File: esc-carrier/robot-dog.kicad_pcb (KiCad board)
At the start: 2 copper layers, 35 parts, among them J1 Conn_01x02, J10 Conn_01x02, J11 Conn_01x04, J12 Conn_01x04, J13 Conn_01x04, J2 Conn_01x04, J3 Conn_01x04, J4 Conn_01x03, J5 Conn_01x05, J6 Conn_01x05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

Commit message: start trace routing
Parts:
- moved R4 43.6 mm to (155.2, 58.4)
- moved R5 43.6 mm to (155.2, 99.1)
- moved R6 43.6 mm to (155.2, 139.7)
- moved SW1 17.2 mm to (195.9, 43.3)
- moved D1 8.64 mm to (213.4, 54.1)
- moved R1 8.64 mm to (213.4, 51.7)
- moved J3 8.62 mm to (185.5, 115.8)
- moved J2 8.62 mm to (185.5, 75.2)
- moved J9 7.95 mm to (183.1, 93.9)
- moved J13 7.88 mm to (192.2, 140.6)
- moved R11 7.88 mm to (209.2, 140.6)
- moved J11 7.88 mm to (192.2, 59.3)
- moved J12 7.88 mm to (192.2, 99.9)
- moved J10 7.88 mm to (183.1, 134.5)
- moved J7 7.88 mm to (181.5, 140.6)
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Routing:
- net +12V: track 0.00 -> 256.4 mm, vias 0 -> 3
- net +5V: track 0.00 -> 251.6 mm, vias 0 -> 5
- net VCC: track 0.00 -> 241.6 mm, vias 0 -> 1
- net SDA: track 0.00 -> 205.1 mm, vias 0 -> 3
- net SCL: track 0.00 -> 196.6 mm, vias 0 -> 3
- net Net-(J11-Pad1): track 0.00 -> 196.4 mm, vias 0 -> 3
- net Net-(J11-Pad2): track 0.00 -> 185.1 mm, vias 0 -> 3
- net Net-(J7-Pad1): track 0.00 -> 27.3 mm
- net Net-(J6-Pad1): track 0.00 -> 26.3 mm
- net Net-(J5-Pad1): track 0.00 -> 26.3 mm
- net Net-(J13-Pad3): track 0.00 -> 18.9 mm
- net Net-(J12-Pad3): track 0.00 -> 18.3 mm
- net Net-(J11-Pad3): track 0.00 -> 18.3 mm
- net Net-(J12-Pad4): track 0.00 -> 14.0 mm
- net Net-(J11-Pad4): track 0.00 -> 14.0 mm
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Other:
- board outline added: 87.6 x 110.5 mm
- board text added: "12V"
- board text added: "5V"
- board text added: "VCC"

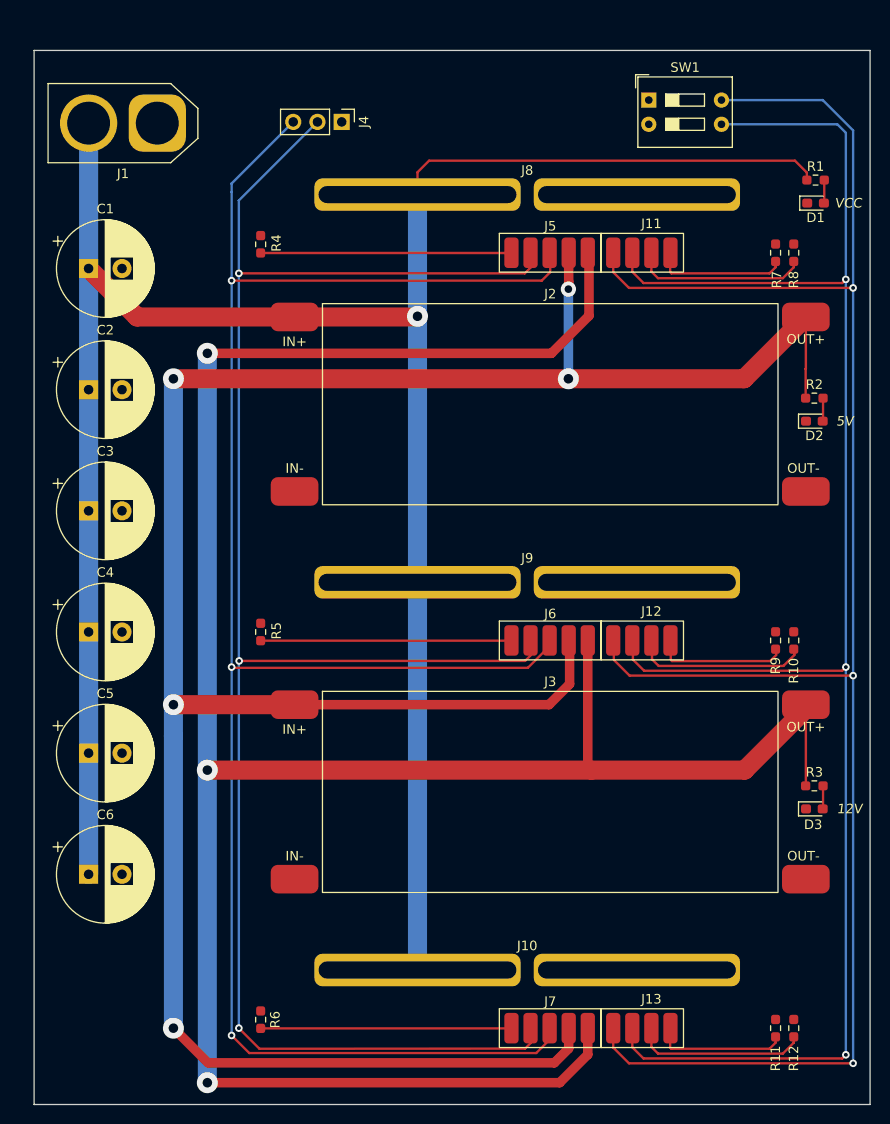
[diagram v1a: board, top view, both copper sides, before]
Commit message: fix intersecting courtyard
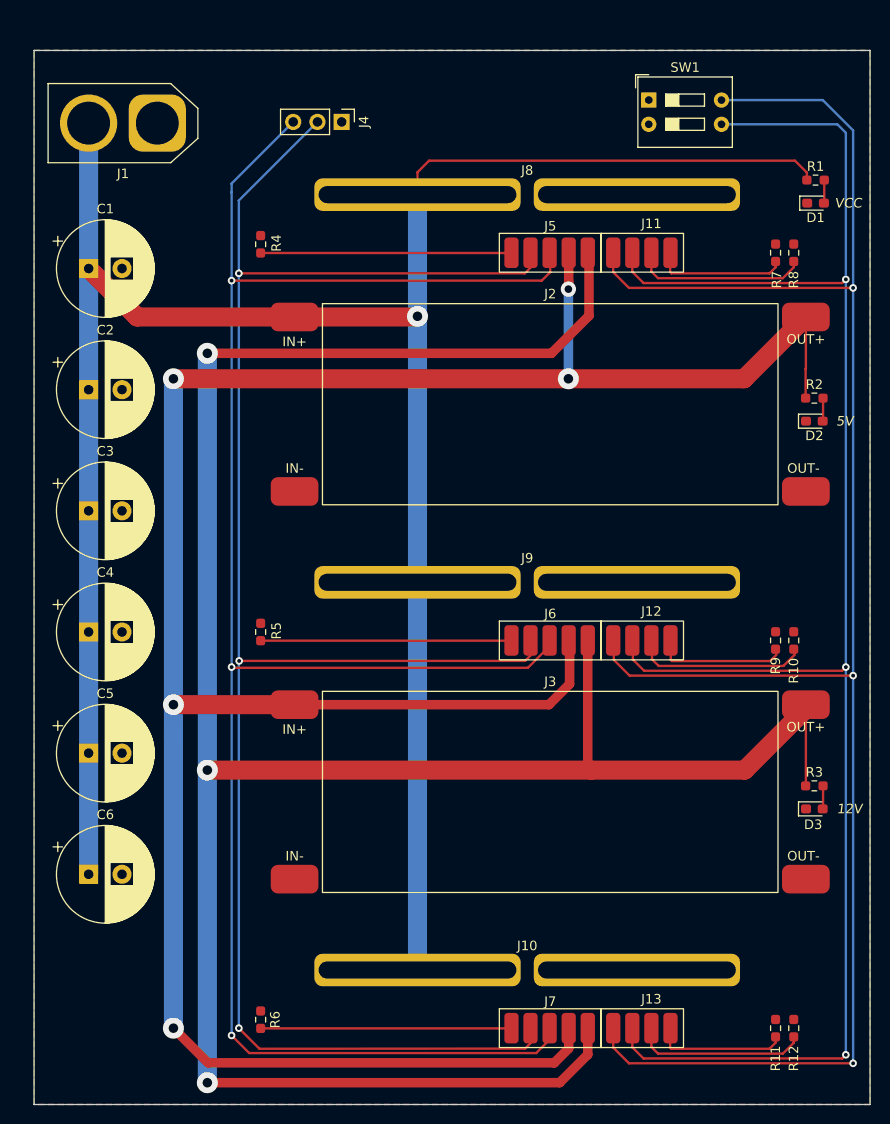
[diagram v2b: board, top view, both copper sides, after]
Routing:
- net Net-(J7-Pad1): track 27.3 -> 26.3 mm
- net Net-(J13-Pad3): track 18.9 -> 18.3 mm
- added copper zone on B.Cu, net GND
- added copper zone on F.Cu, net GND

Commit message: rearrange layout
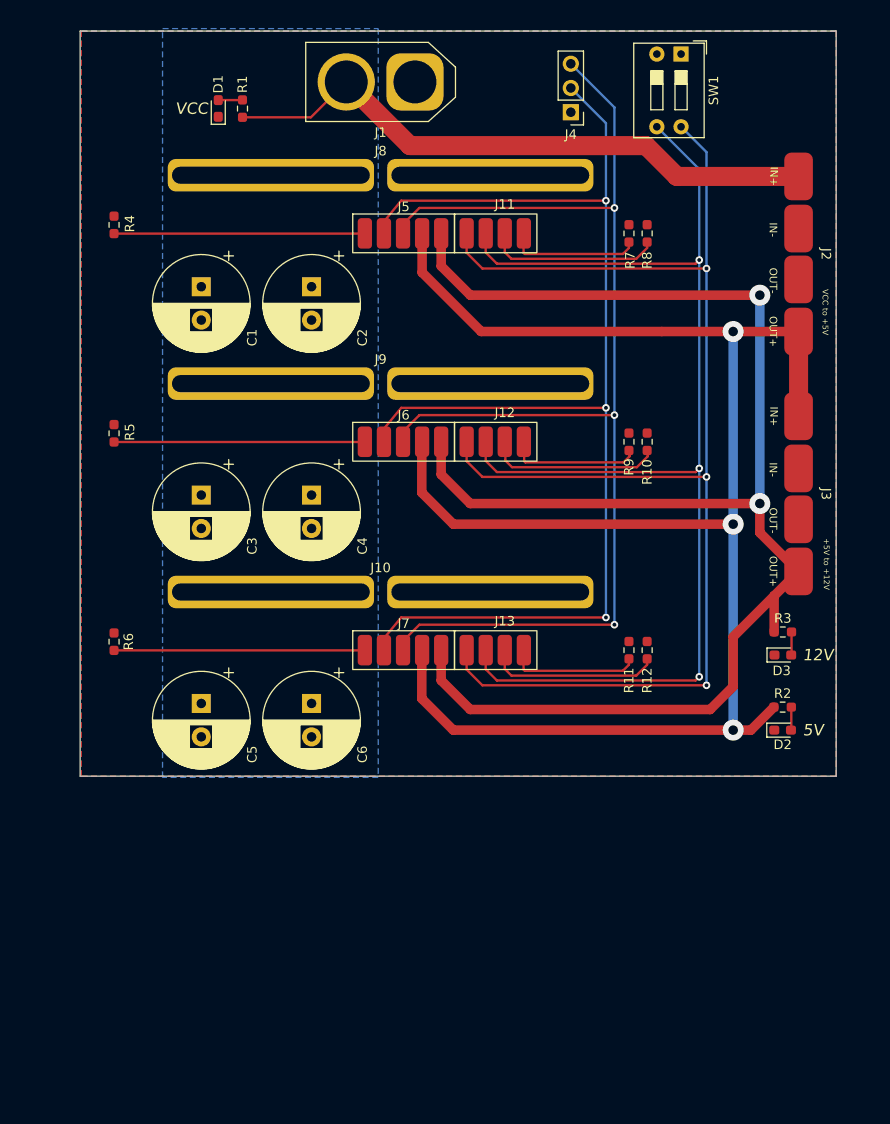
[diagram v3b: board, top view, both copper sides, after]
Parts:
- J2, J3: footprint DogESCCarrier:Converter -> DogESCCarrier:VoltageConverter1
- moved D1 63.4 mm to (150.7, 44.2), turned to 90 degrees
- moved R1 60.5 mm to (153.3, 44.2), turned to 90 degrees
- moved R6 42.5 mm to (139.8, 100.1)
- moved J13 42.5 mm to (176.8, 101.0)
- moved R11 42.5 mm to (193.8, 101.0)
- moved J10 42.5 mm to (167.8, 94.9)
- moved J7 42.5 mm to (166.1, 101.0)
- moved R12 42.5 mm to (195.7, 101.0)
- moved J3 40.7 mm to (211.6, 84.6), turned to -90 degrees
- moved D2 32.6 mm to (209.9, 109.3)
- moved R2 32.6 mm to (209.9, 106.9)
- moved J2 30.4 mm to (211.6, 59.4), turned to -90 degrees
- moved C6 29.4 mm to (160.5, 106.6), turned to -90 degrees
- moved C4 27.4 mm to (160.5, 84.7), turned to -90 degrees
- moved J1 27.4 mm to (171.4, 41.4)
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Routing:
- net VCC: track 241.6 -> 63.9 mm, vias 1 -> 0
- net +12V: track 256.4 -> 161.3 mm, vias 3 -> 2
- net SDA: track 205.1 -> 132.2 mm
- net +5V: track 251.4 -> 180.3 mm, vias 5 -> 3
- net SCL: track 196.5 -> 133.7 mm
- net Net-(J11-Pad1): track 196.4 -> 143.2 mm
- net Net-(J11-Pad2): track 185.1 -> 134.6 mm
- added copper zone on B.Cu, net VCC
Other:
- board size 87.6 x 110.5 mm -> 79.2 x 78.1 mm
- board text added: "+5V to +12V"
- board text added: "VCC to +5V"

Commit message: add vias between gnd planes
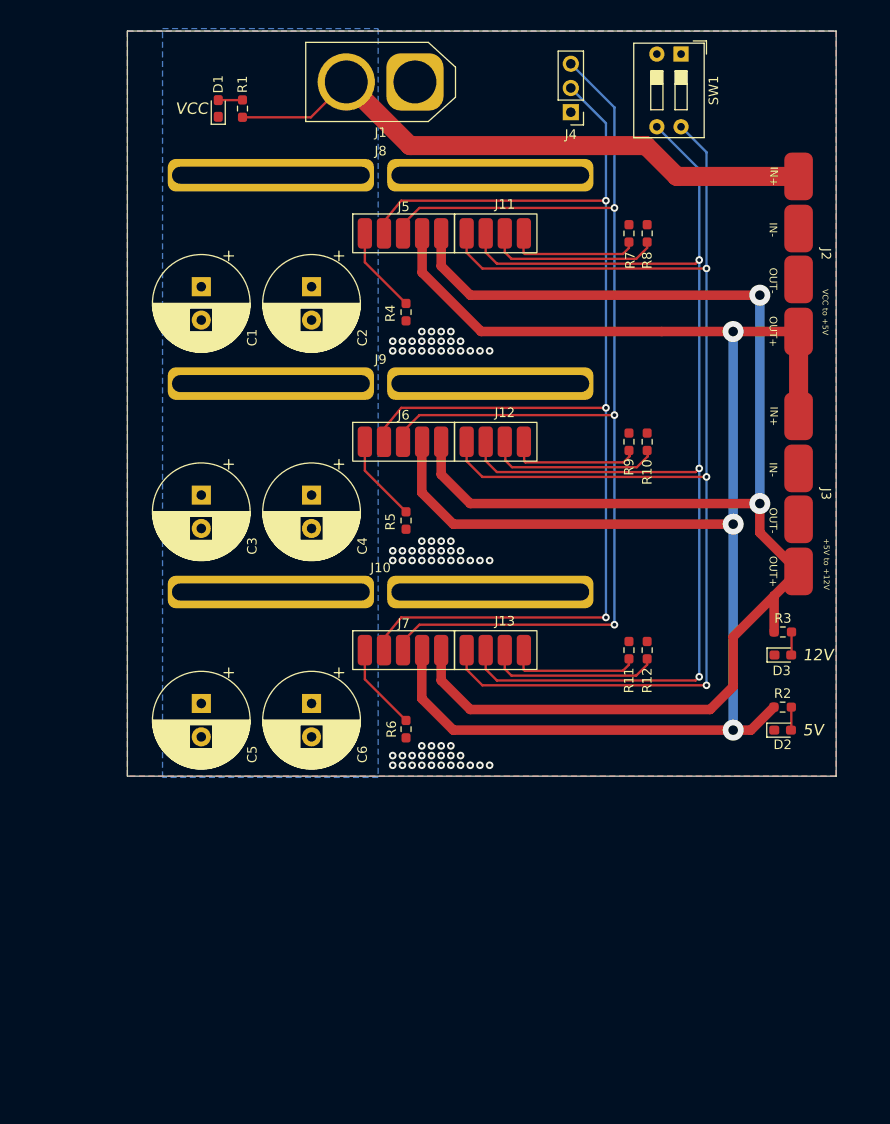
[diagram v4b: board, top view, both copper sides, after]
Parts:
- moved R6 32.0 mm to (170.4, 109.2), turned to -90 degrees
- moved R5 31.9 mm to (170.4, 87.4), turned to -90 degrees
- moved R4 31.9 mm to (170.4, 65.5), turned to -90 degrees
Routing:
- net Net-(J6-Pad1): track 26.3 -> 9.13 mm
- net Net-(J5-Pad1): track 26.3 -> 9.13 mm
- net Net-(J7-Pad1): track 26.3 -> 9.16 mm
- net GND: vias 0 -> 69
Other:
- board size 79.2 x 78.1 mm -> 74.3 x 78.1 mm
